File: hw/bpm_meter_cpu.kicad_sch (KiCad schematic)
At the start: 35 parts, among them J1 USB_C_Receptacle_USB2.0, SW2 SW_MEC_5E, U1 RP2040, U3 W25Q128JVS, U4 AMS1117-3.3, Y1 Crystal_GND24_Small

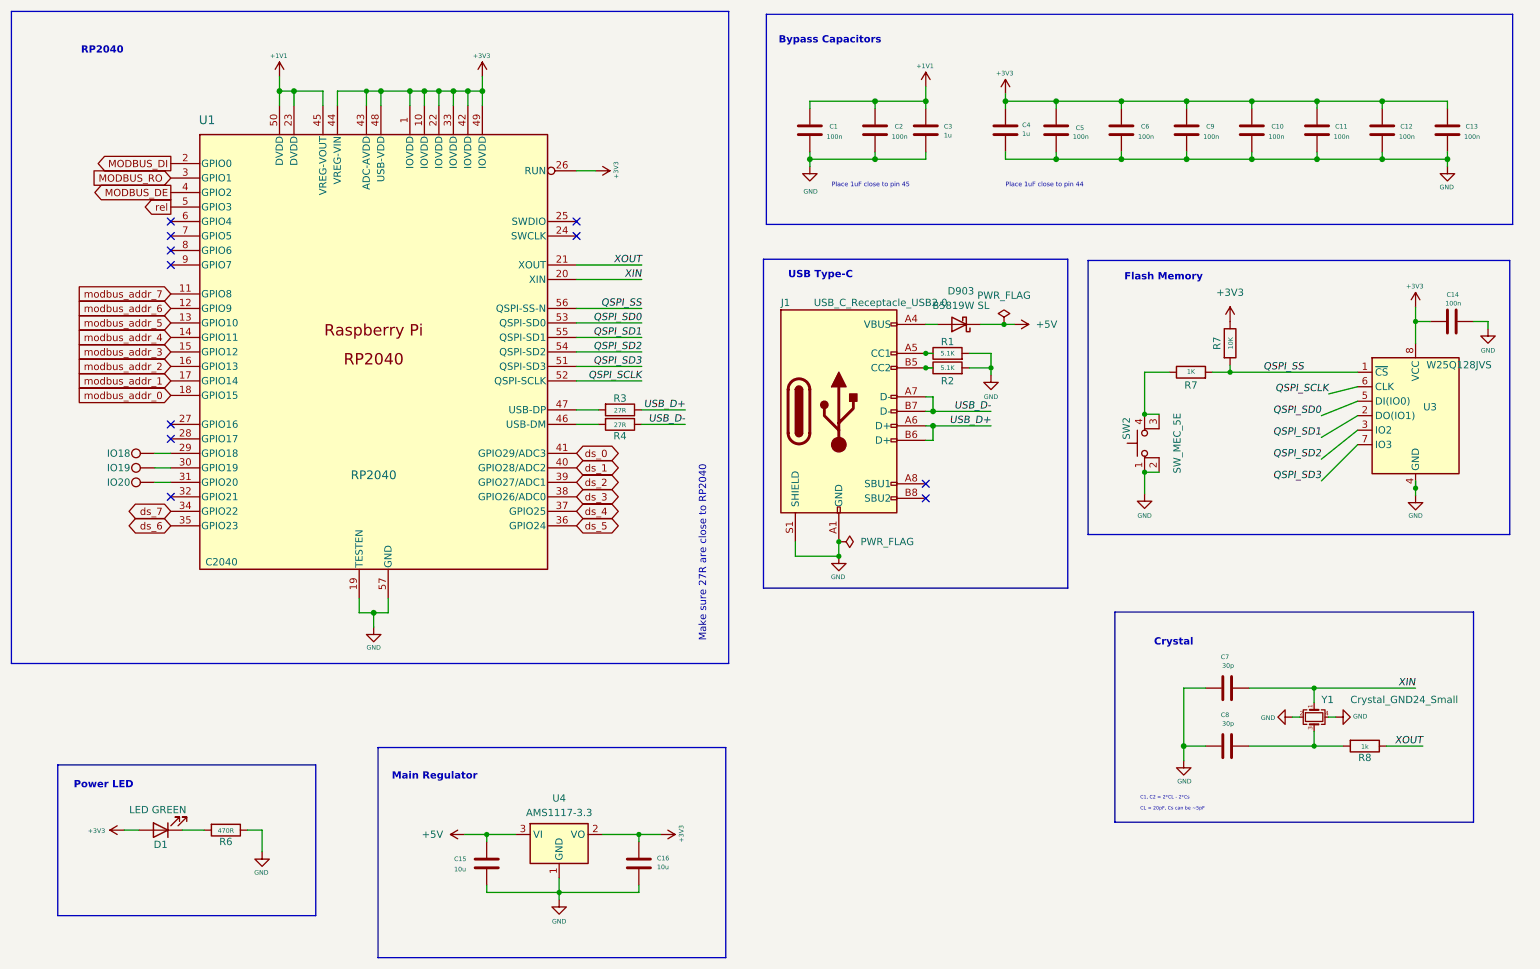
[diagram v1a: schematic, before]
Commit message: Removed unused stuff and added beat input
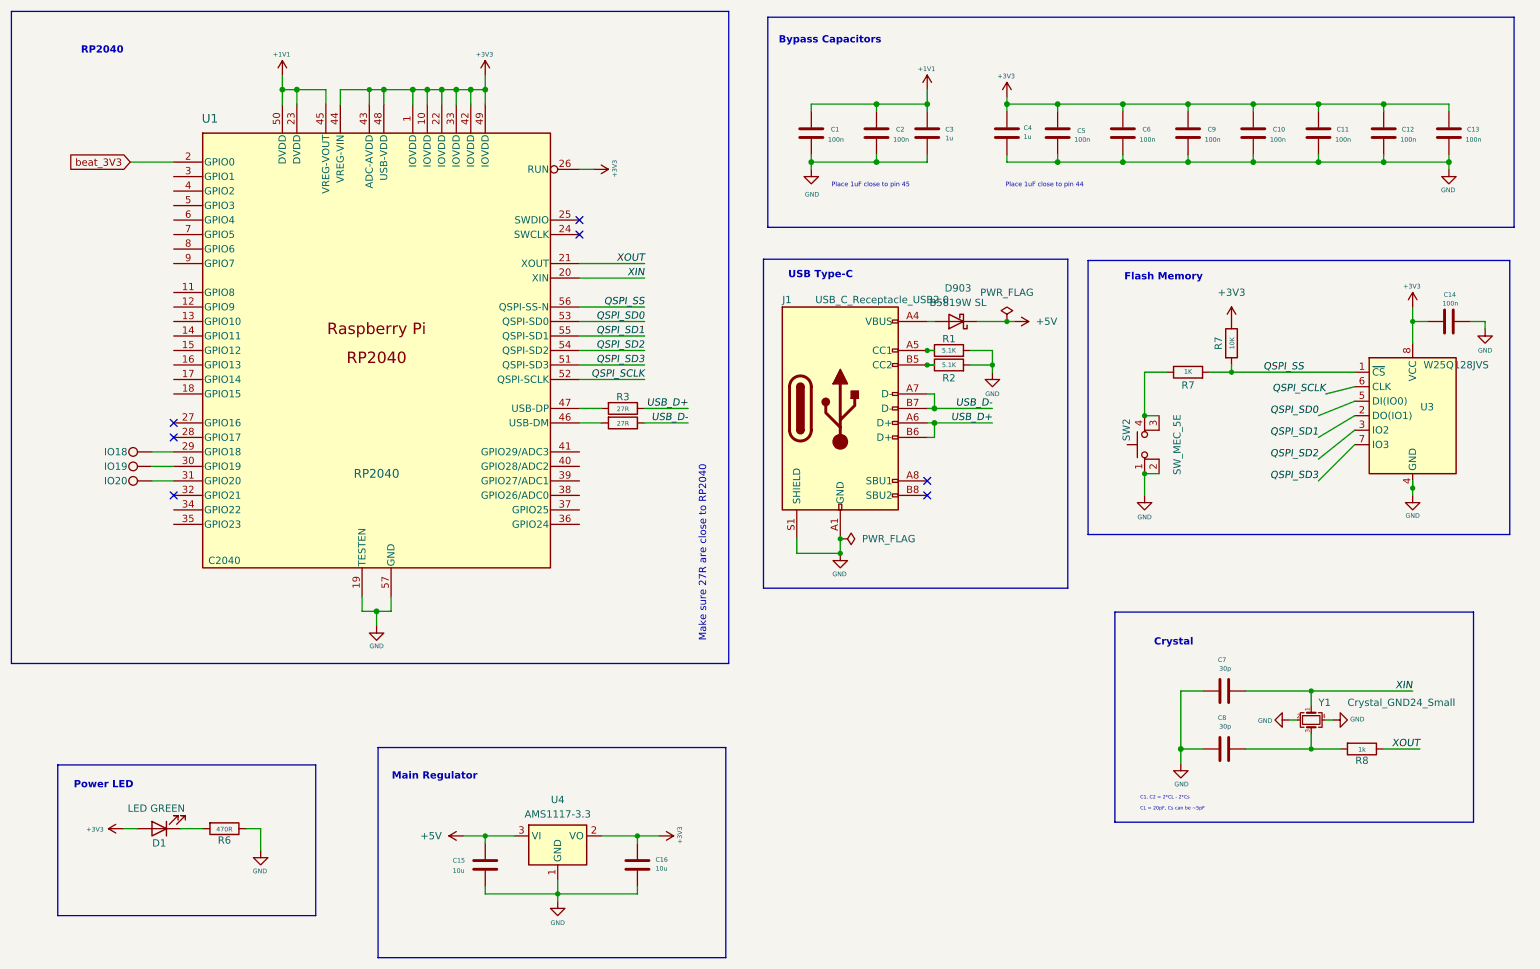
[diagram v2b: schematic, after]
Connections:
- net MODBUS_DE: no longer names the net of U1.4 (GPIO2)
- net MODBUS_DI renamed beat_3V3
- net MODBUS_RO: no longer names the net of U1.3 (GPIO1)
- net ds_0: no longer names the net of U1.41 (GPIO29/ADC3)
- net ds_1: no longer names the net of U1.40 (GPIO28/ADC2)
- net ds_2: no longer names the net of U1.39 (GPIO27/ADC1)
- net ds_3: no longer names the net of U1.38 (GPIO26/ADC0)
- net ds_4: no longer names the net of U1.37 (GPIO25)
- net ds_5: no longer names the net of U1.36 (GPIO24)
- net ds_6: no longer names the net of U1.35 (GPIO23)
- net ds_7: no longer names the net of U1.34 (GPIO22)
- net modbus_addr_0: no longer names the net of U1.18 (GPIO15)
- net modbus_addr_1: no longer names the net of U1.17 (GPIO14)
- net modbus_addr_2: no longer names the net of U1.16 (GPIO13)
- net modbus_addr_3: no longer names the net of U1.15 (GPIO12)
- net modbus_addr_4: no longer names the net of U1.14 (GPIO11)
- net modbus_addr_5: no longer names the net of U1.13 (GPIO10)
- net modbus_addr_6: no longer names the net of U1.12 (GPIO9)
- net modbus_addr_7: no longer names the net of U1.11 (GPIO8)
- net rel: no longer names the net of U1.5 (GPIO3)
- no-connect marks 11 -> 7
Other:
- moved on the sheet: C1, C10, C11, C12, C13, C14, C2, C3, C4, C5, C6, C7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

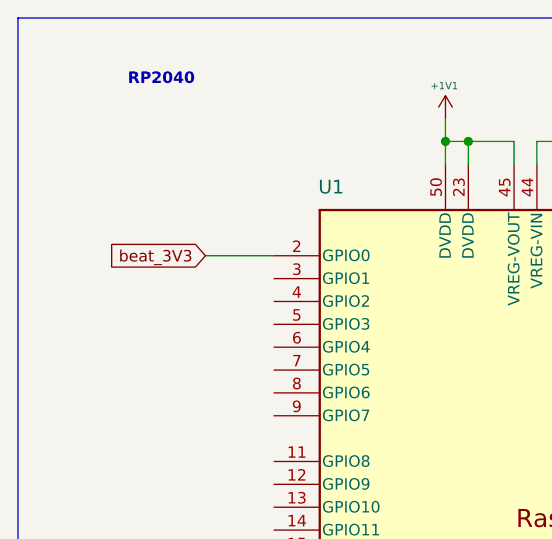
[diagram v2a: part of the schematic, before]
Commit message: Added H11L1 optocoupler to library and schematic
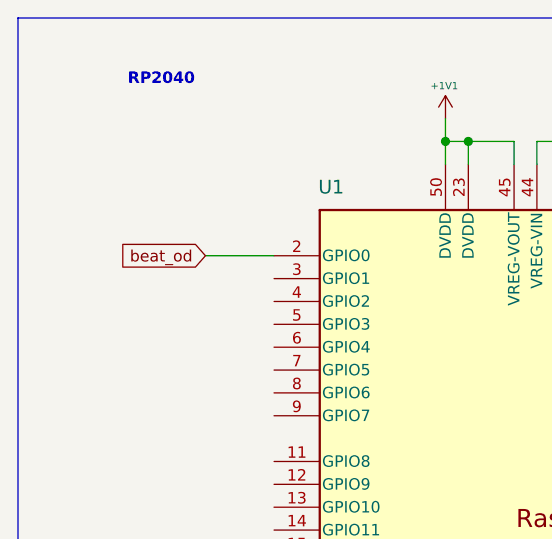
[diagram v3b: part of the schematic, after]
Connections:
- net beat_3V3 renamed beat_od
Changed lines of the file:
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@@
     (effects (font (size 1.27 1.27) italic) (justify right bottom))
   )
-  (global_label "beat_3V3" (shape input) (at 36.83 41.91 180) (fields_autoplaced)
+  (global_label "beat_od" (shape input) (at 36.83 41.91 180) (fields_autoplaced)
     (effects (font (size 1.27 1.27)) (justify right))
-    (property "Intersheetrefs" "${INTERSHEET_REFS}" (at 25.1622 41.91 0)
+    (property "Intersheetrefs" "${INTERSHEET_REFS}" (at 26.3718 41.91 0)
       (effects (font (size 1.27 1.27)) (justify right) hide)
     )

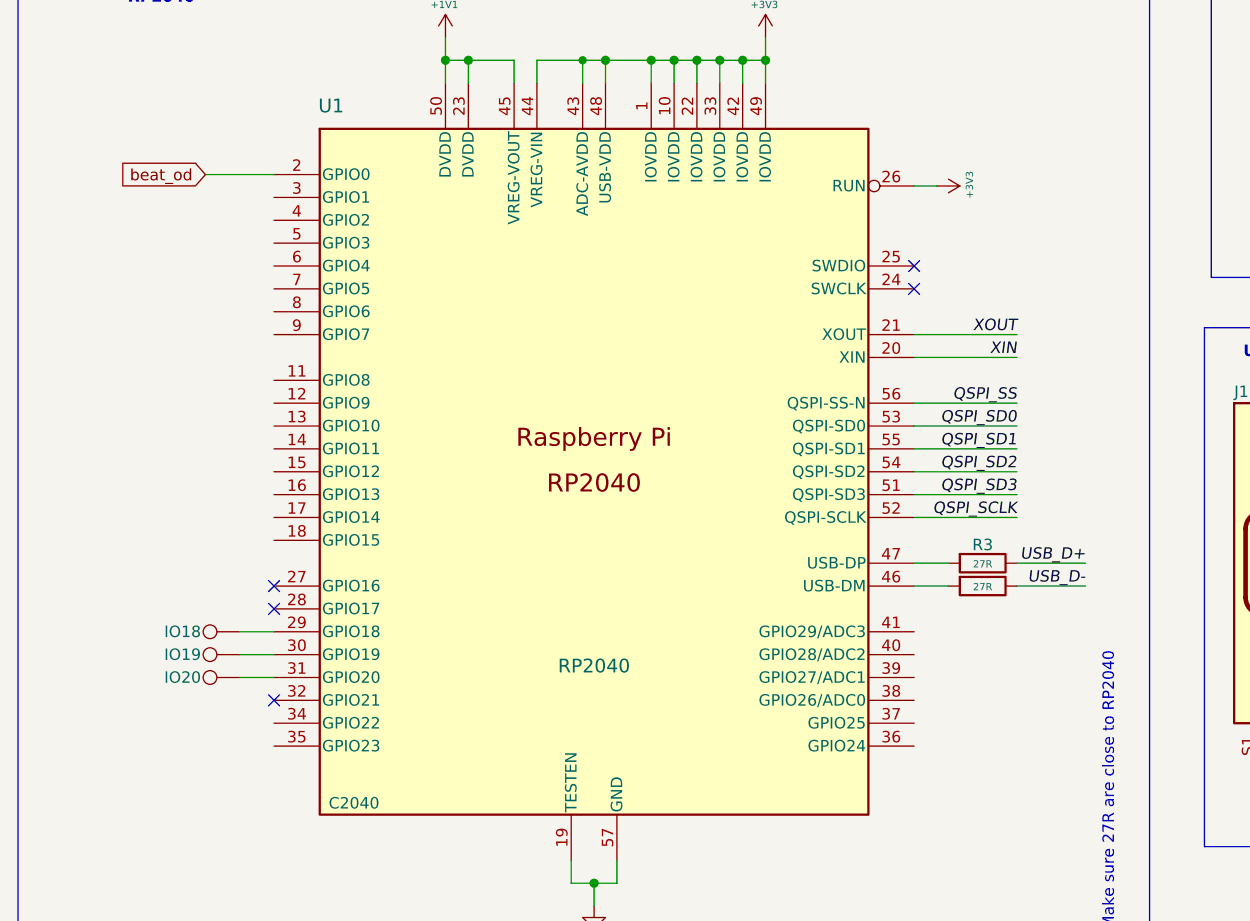
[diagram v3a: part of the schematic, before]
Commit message: Connected the segment displays using dual FETs
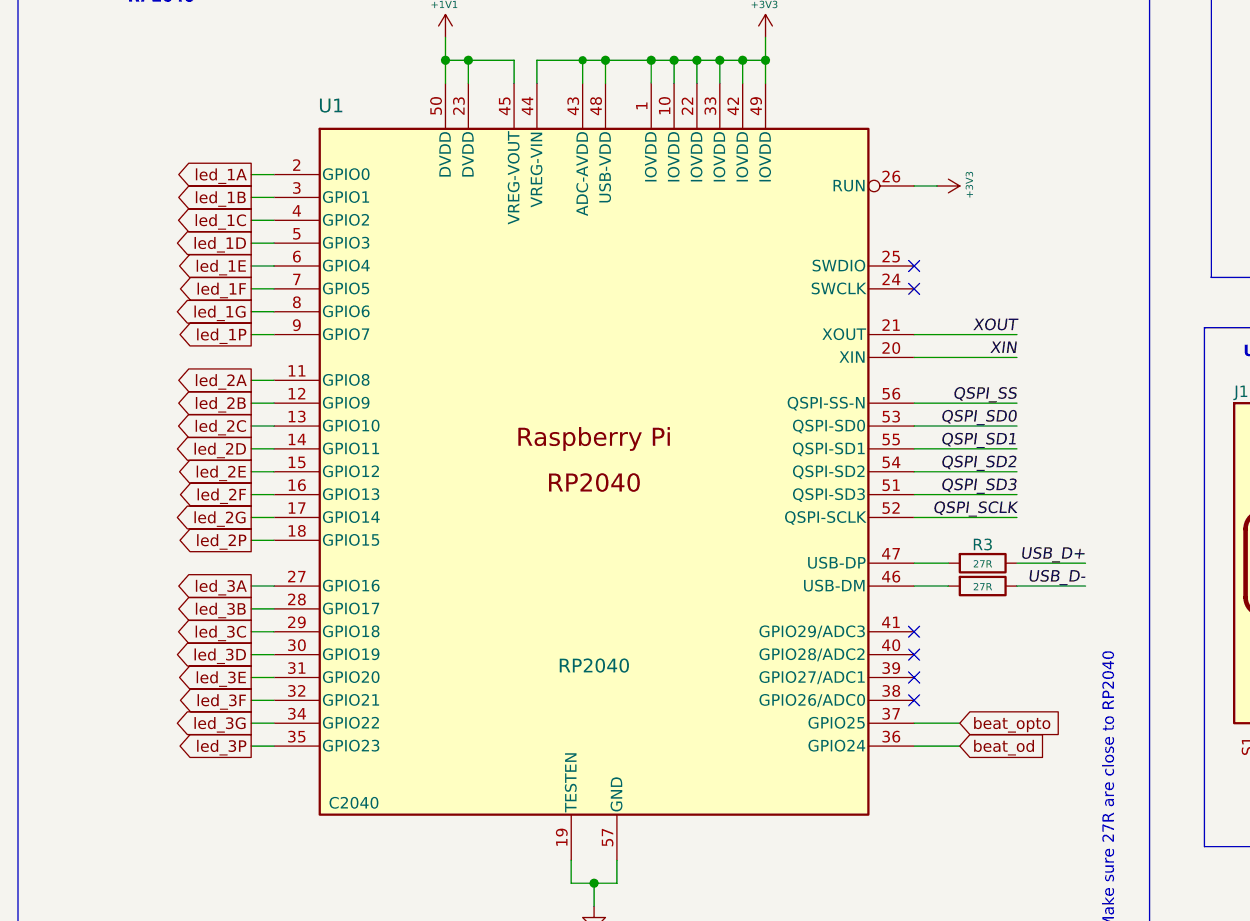
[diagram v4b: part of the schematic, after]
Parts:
- removed IO18, IO19, IO20: TestPoint, TestPoint:TestPoint_Pad_D1.0mm, symbol Connector:TestPoint
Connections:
- net beat_od: now also U1.36 (GPIO24); no longer U1.2 (GPIO0)
- net led_3D: now reaches U1.30 (GPIO19)
- net led_2A: now reaches U1.11 (GPIO8)
- net led_2B: now reaches U1.12 (GPIO9)
- net led_2C: now reaches U1.13 (GPIO10)
- net led_2D: now reaches U1.14 (GPIO11)
- net led_2E: now reaches U1.15 (GPIO12)
- net led_2F: now reaches U1.16 (GPIO13)
- net led_2G: now reaches U1.17 (GPIO14)
- net led_2P: now reaches U1.18 (GPIO15)
- net led_3A: now reaches U1.27 (GPIO16)
- net led_3B: now reaches U1.28 (GPIO17)
- net led_3C: now reaches U1.29 (GPIO18)
- net led_1B: now reaches U1.3 (GPIO1)
- net led_3E: now reaches U1.31 (GPIO20)
- net led_3F: now reaches U1.32 (GPIO21)
- net led_3G: now reaches U1.34 (GPIO22)
- net led_3P: now reaches U1.35 (GPIO23)
- net beat_opto: now reaches U1.37 (GPIO25)
- net led_1C: now reaches U1.4 (GPIO2)
- net led_1D: now reaches U1.5 (GPIO3)
- net led_1E: now reaches U1.6 (GPIO4)
- net led_1F: now reaches U1.7 (GPIO5)
- net led_1G: now reaches U1.8 (GPIO6)
- net led_1P: now reaches U1.9 (GPIO7)
- new net led_1A: U1.2 (GPIO0)
- no-connect marks 7 -> 8

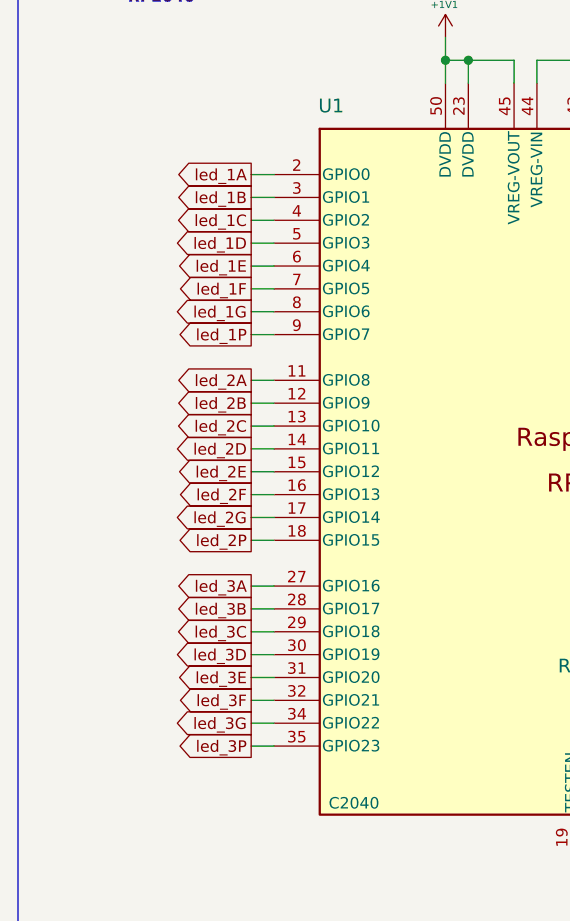
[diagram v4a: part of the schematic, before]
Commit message: Now using LP5030 LED driver
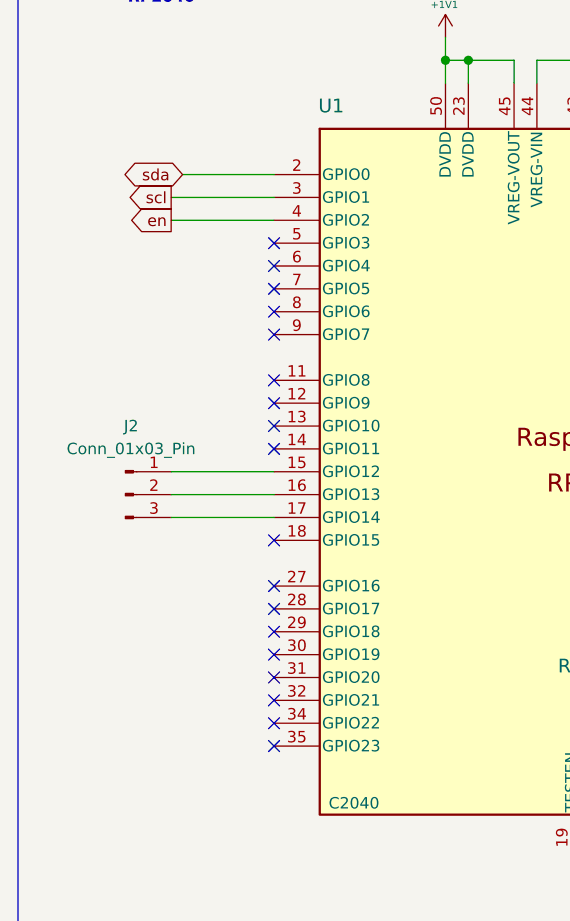
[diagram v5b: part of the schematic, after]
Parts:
- added J2: Conn_01x03_Pin, Connector_PinHeader_2.54mm:PinHeader_1x03_P2.54mm_Vertical, symbol Connector:Conn_01x03_Pin
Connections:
- net led_1A renamed sda
- net led_1B renamed scl
- net led_1C renamed en
- net led_1D: no longer names the net of U1.5 (GPIO3)
- net led_1E: no longer names the net of U1.6 (GPIO4)
- net led_1F: no longer names the net of U1.7 (GPIO5)
- net led_1G: no longer names the net of U1.8 (GPIO6)
- net led_1P: no longer names the net of U1.9 (GPIO7)
- net led_2A: no longer names the net of U1.11 (GPIO8)
- net led_2B: no longer names the net of U1.12 (GPIO9)
- net led_2C: no longer names the net of U1.13 (GPIO10)
- net led_2D: no longer names the net of U1.14 (GPIO11)
- net led_2E: no longer names the net of U1.15 (GPIO12)
- net led_2E: now also J2.1 (Pin_1)
- net led_2F: no longer names the net of U1.16 (GPIO13)
- net led_2F: now also J2.2 (Pin_2)
- net led_2G: no longer names the net of U1.17 (GPIO14)
- net led_2G: now also J2.3 (Pin_3)
- net led_2P: no longer names the net of U1.18 (GPIO15)
- net led_3A: no longer names the net of U1.27 (GPIO16)
- net led_3B: no longer names the net of U1.28 (GPIO17)
- net led_3C: no longer names the net of U1.29 (GPIO18)
- net led_3D: no longer names the net of U1.30 (GPIO19)
- net led_3E: no longer names the net of U1.31 (GPIO20)
- net led_3F: no longer names the net of U1.32 (GPIO21)
- net led_3G: no longer names the net of U1.34 (GPIO22)
- net led_3P: no longer names the net of U1.35 (GPIO23)
- no-connect marks 8 -> 26
